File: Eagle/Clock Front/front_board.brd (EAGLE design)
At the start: 14 parts

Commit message: New front board revision
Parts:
- removed E$3, E$4: (no value), rcl:0309/12
- added E$5, E$6: (no value), rcl:0309/20
- moved R1 0.63 mm to (-14.0, -15.2)
- moved R2 0.63 mm to (14.0, -15.2)
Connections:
- new net +200V_LEFT: E$5.1
- new net +200V_RIGHT: E$6.2
- net +200V: no longer E$3.1, E$4.2
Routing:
- net S$13: track 19.7 -> 0.00 mm, vias 1 -> 0
- net S$12: track 40.8 -> 59.7 mm, vias 1 -> 2
- net S$3: track 51.6 -> 33.8 mm
- net S$8: track 37.9 -> 21.7 mm, vias 0 -> 2
- net S$22: track 61.1 -> 48.4 mm
- net +200V_LEFT: track 14.0 -> 21.9 mm
- net +200V_RIGHT: track 7.51 -> 14.6 mm
- net LED+: track 86.6 -> 81.7 mm
- net GND_LOW: track 157.1 -> 152.3 mm
- net S$21: track 15.3 -> 18.7 mm
- net S$20: track 23.6 -> 25.3 mm
- net S$10: track 16.0 -> 17.6 mm
- net S$14: track 42.2 -> 41.3 mm
- net S$25: track 21.3 -> 22.0 mm
- net S$23: track 31.5 -> 30.8 mm
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
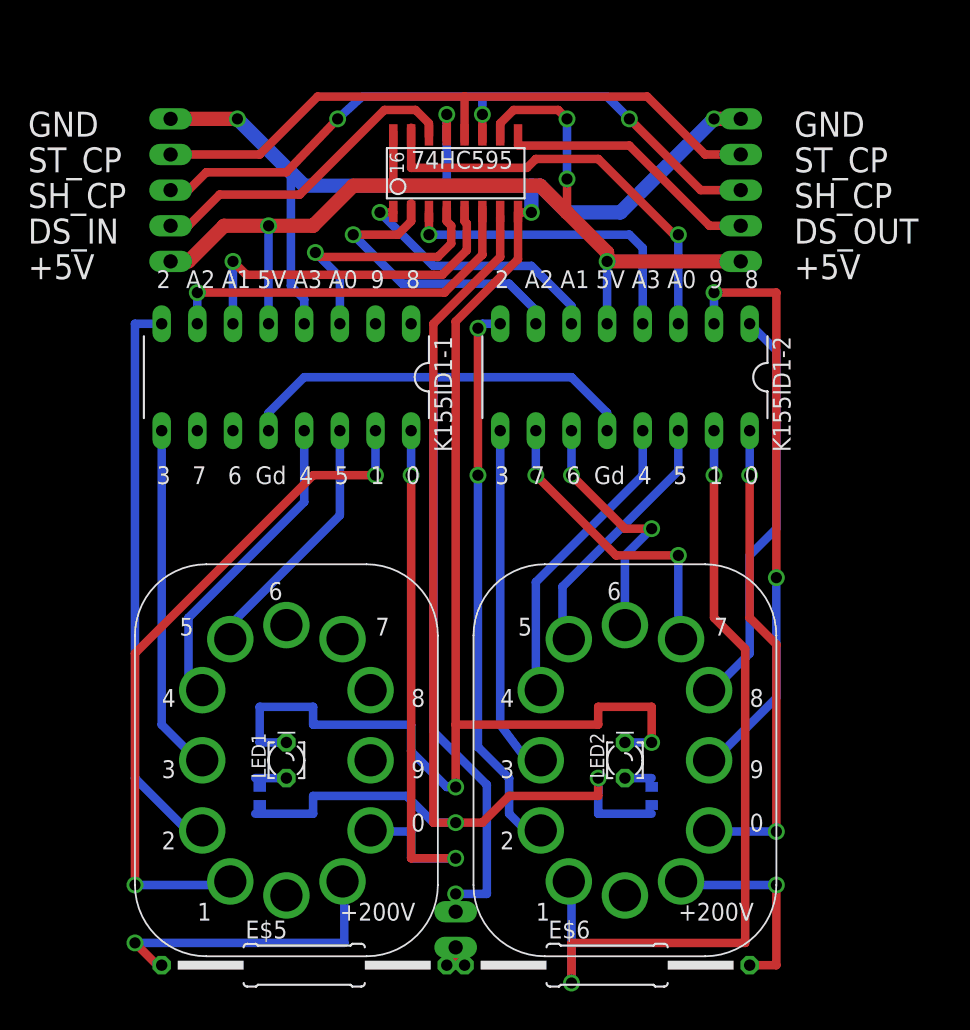
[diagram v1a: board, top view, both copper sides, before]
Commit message: Minor enhancements; Polygons added
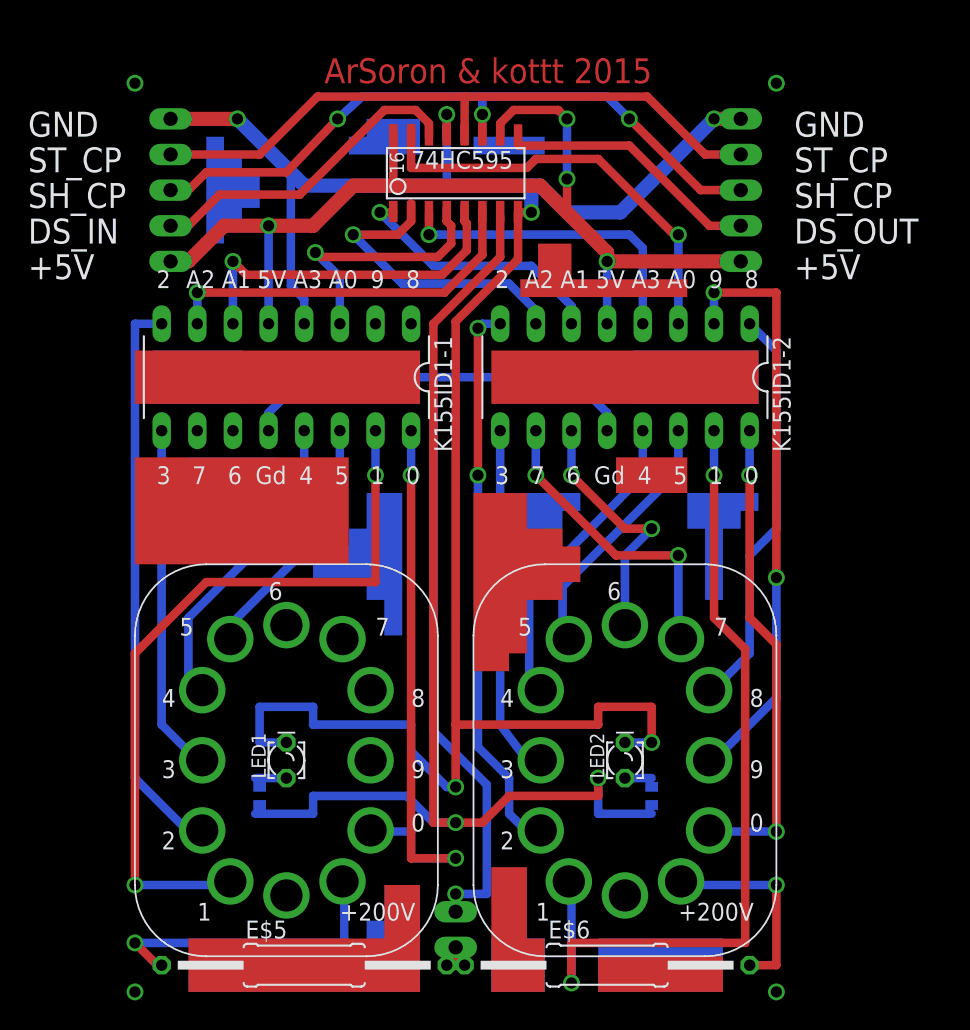
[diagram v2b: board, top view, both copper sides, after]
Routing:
- net S$22: track 48.4 -> 52.9 mm
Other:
- board text added: "ArSoron & kottt 2015"

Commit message: Схема: переделаны отверстия на 1.0 мм; Ардуино - вырезана работа с кнопкой (глючит)
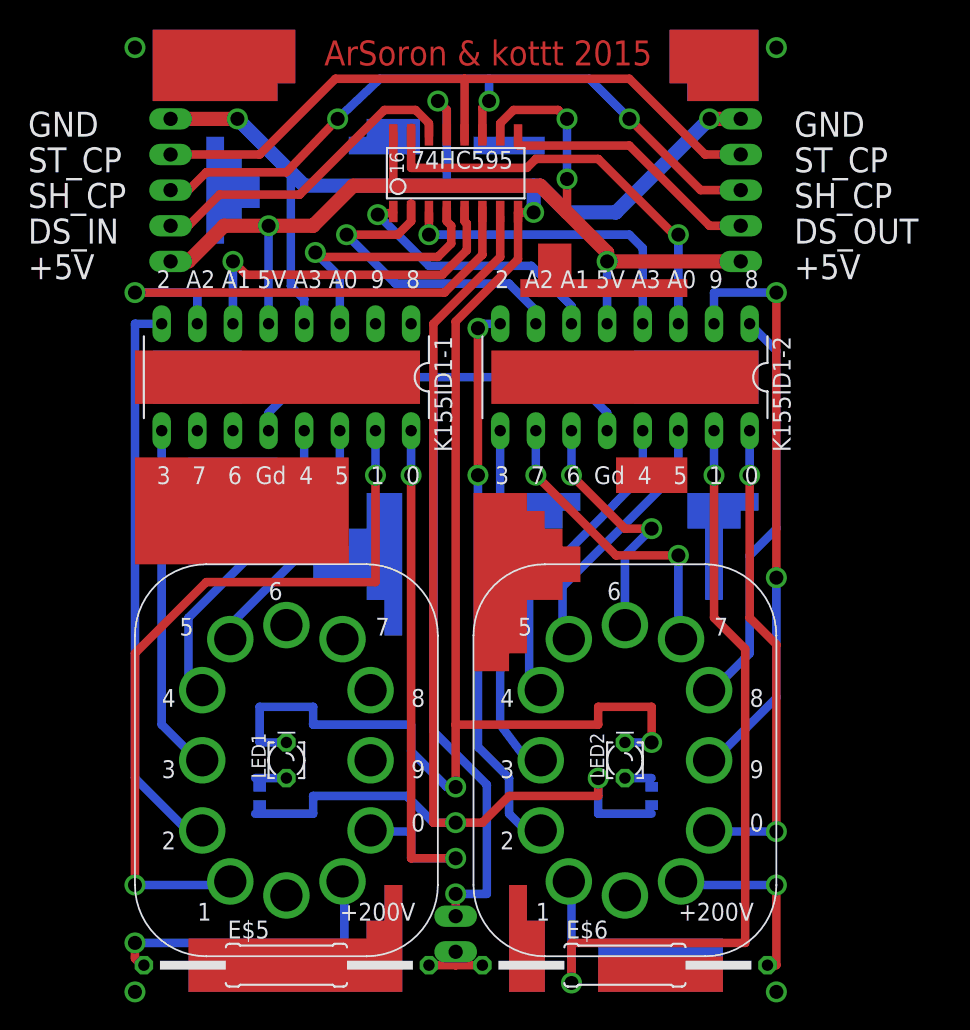
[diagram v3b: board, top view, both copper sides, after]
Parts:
- moved E$5 1.27 mm to (-12.1, -27.3)
- moved E$6 1.27 mm to (12.1, -27.3)
- moved 200VCONNECTOR 0.32 mm to (0.00, -25.1)
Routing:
- net S$9: track 27.0 -> 35.9 mm
- net GND_LOW: track 152.3 -> 154.9 mm
- net SH_CP: track 49.3 -> 51.9 mm
- net ST_CP: track 47.2 -> 49.6 mm
- net +200V: track 2.54 -> 4.76 mm
- net +200V_RIGHT: track 14.6 -> 13.3 mm
- net S$25: track 22.0 -> 23.0 mm
- net +200V_LEFT: track 21.9 -> 21.3 mm
